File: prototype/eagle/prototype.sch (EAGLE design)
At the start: 45 parts, among them J4 USBSMD, T1 3904, U1 ATMEGA328, U2 ATA6631, U3 ATA6631, U5 FT232RL, X1 16MHz

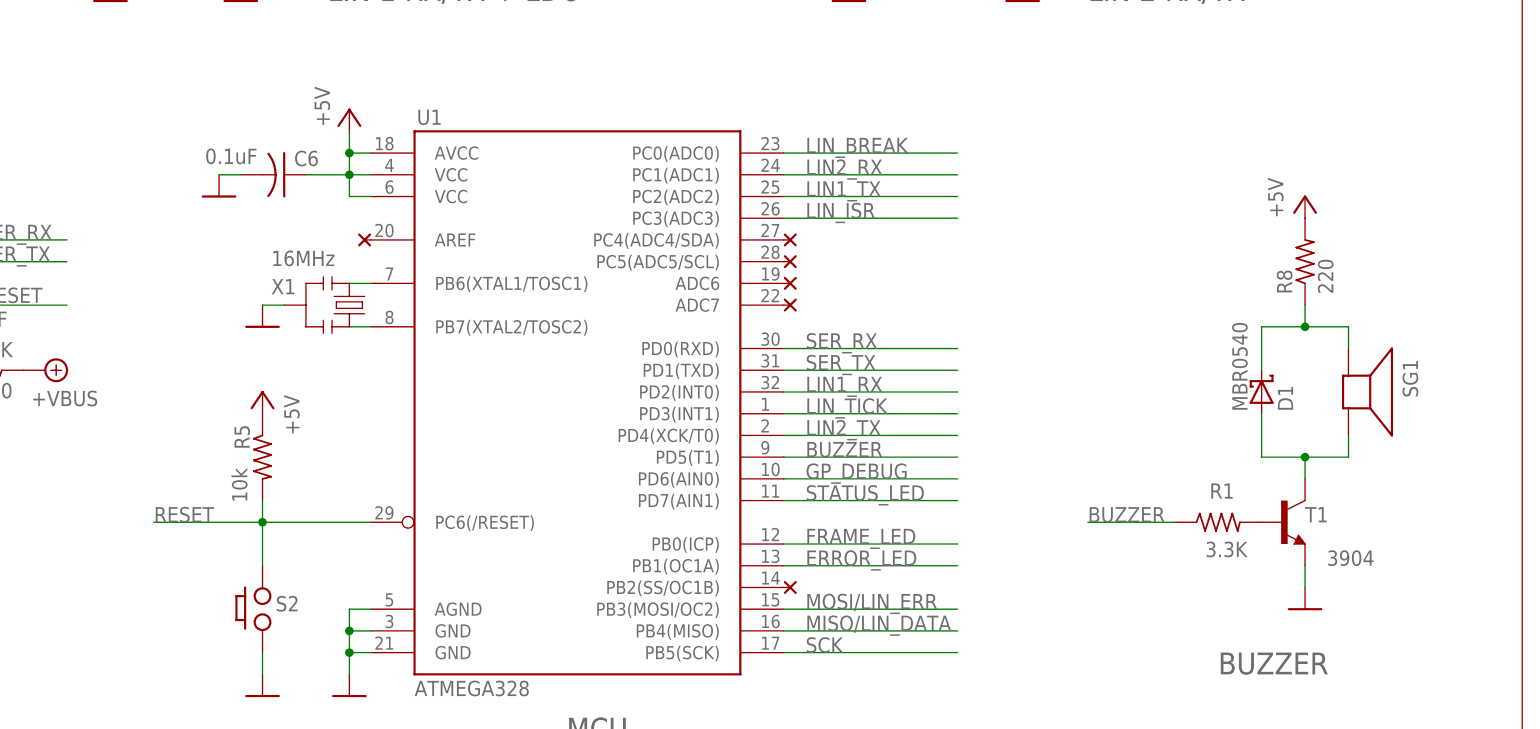
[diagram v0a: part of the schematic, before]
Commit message: Updated prototype schema. Buzzer is now fed from 12V (was 5V).
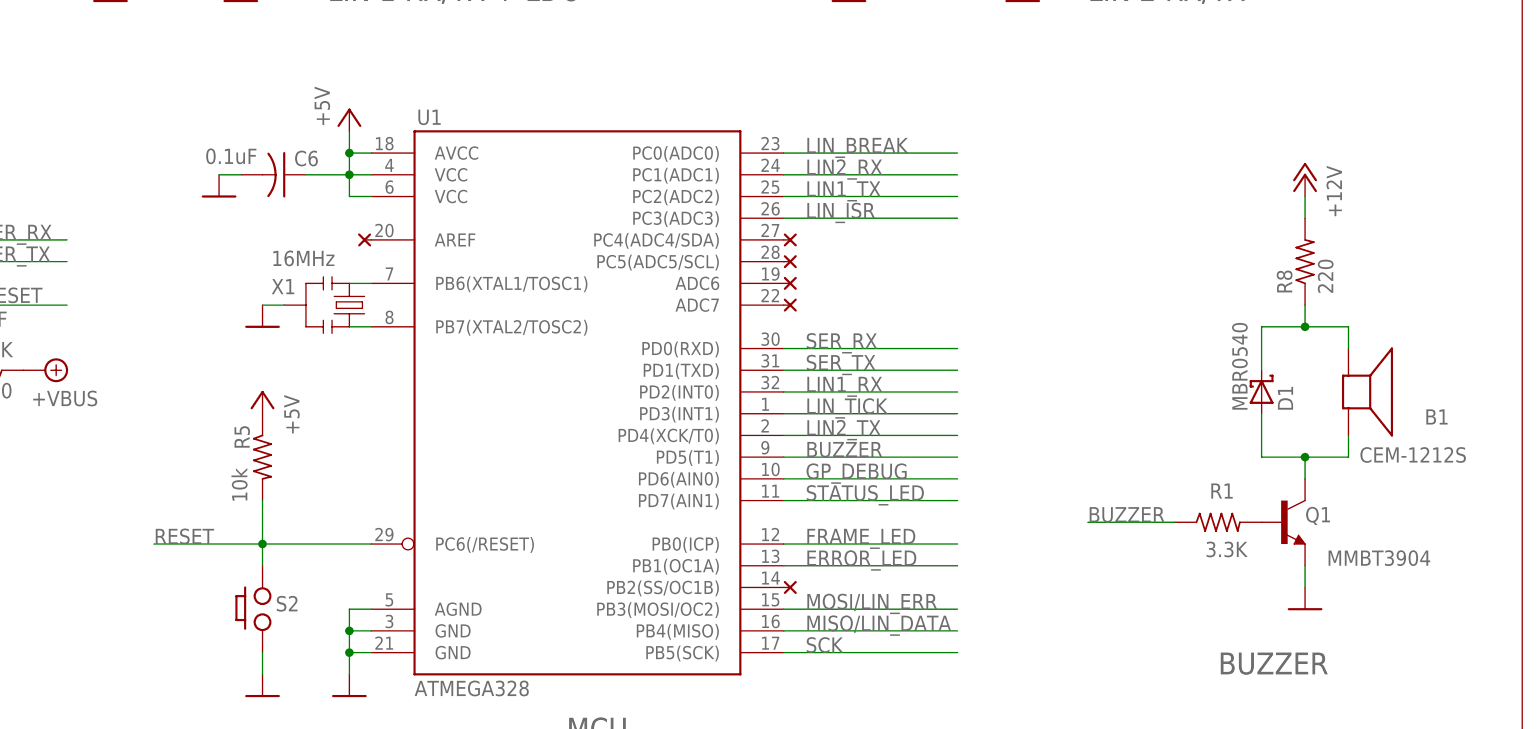
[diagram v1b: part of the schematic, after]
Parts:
- B1: value AL60P -> CEM-1212S
- Q1: value 3904 -> MMBT3904
- renumbered SG1 to B1, T1 to Q1
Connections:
- net +12V: now also R8.2
- net +5V: no longer R8.2
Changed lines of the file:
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@@
 <part name="GND14" library="prototype" deviceset="GND" device=""/>
 <part name="P+5" library="prototype" deviceset="+5V" device=""/>
-<part name="SG1" library="prototype" deviceset="AL60P" device="" value=""/>
+<part name="B1" library="prototype" deviceset="AL60P" device="" value="CEM-1212S"/>
 <part name="R1" library="prototype" deviceset="R-US_" device="R0805" value="3.3K"/>
-<part name="T1" library="prototype" deviceset="*-NPN-" device="SOT23-BEC" technology="MMBT3904LT1" value="3904"/>
+<part name="Q1" library="prototype" deviceset="*-NPN-" device="SOT23-BEC" technology="MMBT3904LT1" value="MMBT3904"/>
 <part name="GND18" library="prototype" deviceset="GND" device=""/>
 <part name="D1" library="prototype" deviceset="SMF5.0AT1" device="" value="MBR0540"/>
-<part name="P+3" library="prototype" deviceset="+5V" device=""/>
 <part name="R8" library="prototype" deviceset="R-US_" device="R0805" value="220"/>
 <part name="GND10" library="prototype" deviceset="GND" device=""/>
@@
 <part name="C6" library="prototype" deviceset="C-US" device="C0805" value="0.1uF"/>
 <part name="GND30" library="prototype" deviceset="GND" device=""/>
+<part name="P+3" library="prototype" deviceset="+12V" device=""/>
 </parts>
 <sheets>
@@
 <attribute name="VALUE" x="190.5" y="60.198" size="1.778" layer="96" rot="MR90"/>
 </instance>
-<instance part="SG1" gate="G$1" x="289.56" y="114.3" rot="R270"/>
+<instance part="B1" gate="G$1" x="289.56" y="114.3" smashed="yes" rot="R270">
+<attribute name="NAME" x="298.45" y="110.49" size="1.778" layer="95"/>
+<attribute name="VALUE" x="290.83" y="106.045" size="1.778" layer="96"/>
+</instance>
 <instance part="R1" gate="G$1" x="274.32" y="99.06" smashed="yes">
 <attribute name="NAME" x="273.304" y="101.8286" size="1.778" layer="95"/>
 <attribute name="VALUE" x="272.796" y="94.996" size="1.778" layer="96"/>
 </instance>
-<instance part="T1" gate="G$1" x="281.94" y="99.06" smashed="yes">
+<instance part="Q1" gate="G$1" x="281.94" y="99.06" smashed="yes">
 <attribute name="NAME" x="284.48" y="99.06" size="1.778" layer="95"/>
 <attribute name="VALUE" x="287.02" y="93.98" size="1.778" layer="96"/>
@@
 <instance part="GND18" gate="1" x="284.48" y="88.9"/>
 <instance part="D1" gate="G$1" x="279.4" y="114.3" rot="MR90"/>
-<instance part="P+3" gate="1" x="284.48" y="137.16" smashed="yes">
-<attribute name="VALUE" x="281.94" y="134.62" size="1.778" layer="96" rot="R90"/>
-</instance>
 <instance part="R8" gate="G$1" x="284.48" y="129.54" rot="R90"/>
 <instance part="GND10" gate="1" x="160.02" y="160.02"/>
@@
 </instance>
 <instance part="GND30" gate="1" x="157.48" y="137.16"/>
+<instance part="P+3" gate="1" x="284.48" y="139.7" rot="MR0"/>
 </instances>
 <busses>
@@
 </segment>
 <segment>
-<pinref part="T1" gate="G$1" pin="E"/>
+<pinref part="Q1" gate="G$1" pin="E"/>
 <pinref part="GND18" gate="1" pin="GND"/>
 <wire x1="284.48" y1="93.98" x2="284.48" y2="91.44" width="0.1524" layer="91"/>
@@
 <wire x1="111.76" y1="152.4" x2="119.38" y2="152.4" width="0.1524" layer="91"/>
 </segment>
+<segment>
+<pinref part="P+3" gate="1" pin="+12V"/>
+<pinref part="R8" gate="G$1" pin="2"/>
+<wire x1="284.48" y1="137.16" x2="284.48" y2="134.62" width="0.1524" layer="91"/>
+</segment>
 </net>
 <net name="+5V" class="0">
@@
 <wire x1="177.8" y1="58.42" x2="187.96" y2="58.42" width="0.1524" layer="91"/>
 <wire x1="187.96" y1="58.42" x2="187.96" y2="60.96" width="0.1524" layer="91"/>
-</segment>
-<segment>
-<pinref part="P+3" gate="1" pin="+5V"/>
-<pinref part="R8" gate="G$1" pin="2"/>
 </segment>
 <segment>
@@
 <pinref part="D1" gate="G$1" pin="A"/>
 <wire x1="279.4" y1="111.76" x2="279.4" y2="106.68" width="0.1524" layer="91"/>
-<pinref part="T1" gate="G$1" pin="C"/>
+<pinref part="Q1" gate="G$1" pin="C"/>
 <wire x1="279.4" y1="106.68" x2="284.48" y2="106.68" width="0.1524" layer="91"/>
 <wire x1="284.48" y1="106.68" x2="284.48" y2="104.14" width="0.1524" layer="91"/>
-<pinref part="SG1" gate="G$1" pin="2"/>
+<pinref part="B1" gate="G$1" pin="2"/>
 <wire x1="284.48" y1="106.68" x2="289.56" y2="106.68" width="0.1524" layer="91"/>
 <wire x1="289.56" y1="106.68" x2="289.56" y2="109.22" width="0.1524" layer="91"/>
@@
 <net name="N$19" class="0">
 <segment>
-<pinref part="T1" gate="G$1" pin="B"/>
+<pinref part="Q1" gate="G$1" pin="B"/>
 <pinref part="R1" gate="G$1" pin="2"/>
 </segment>
@@
 <pinref part="D1" gate="G$1" pin="C"/>
 <wire x1="279.4" y1="116.84" x2="279.4" y2="121.92" width="0.1524" layer="91"/>
-<pinref part="SG1" gate="G$1" pin="1"/>
+<pinref part="B1" gate="G$1" pin="1"/>
 <wire x1="279.4" y1="121.92" x2="284.48" y2="121.92" width="0.1524" layer="91"/>
 <wire x1="284.48" y1="121.92" x2="289.56" y2="121.92" width="0.1524" layer="91"/>
@@
 <segment>
 <pinref part="U1" gate="G$1" pin="PC6(/RESET)"/>
-<wire x1="175.26" y1="99.06" x2="162.56" y2="99.06" width="0.1524" layer="91"/>
+<wire x1="175.26" y1="96.52" x2="162.56" y2="96.52" width="0.1524" layer="91"/>
 <pinref part="R5" gate="G$1" pin="2"/>
 <pinref part="S2" gate="G$1" pin="P$3"/>
-<wire x1="162.56" y1="99.06" x2="149.86" y2="99.06" width="0.1524" layer="91"/>
-<wire x1="162.56" y1="101.6" x2="162.56" y2="99.06" width="0.1524" layer="91"/>
-<junction x="162.56" y="99.06"/>
-<wire x1="162.56" y1="99.06" x2="162.56" y2="93.98" width="0.1524" layer="91"/>
-<label x="149.86" y="99.06" size="1.778" layer="95"/>
-</segment>
-</net>
+<wire x1="162.56" y1="96.52" x2="149.86" y2="96.52" width="0.1524" layer="91"/>
+<wire x1="162.56" y1="101.6" x2="162.56" y2="96.52" width="0.1524" layer="91"/>
+<junction x="162.56" y="96.52"/>
+<wire x1="162.56" y1="96.52" x2="162.56" y2="93.98" width="0.1524" layer="91"/>
+<label x="149.86" y="96.52" size="1.778" layer="95"/>
+</segment>
+</net>

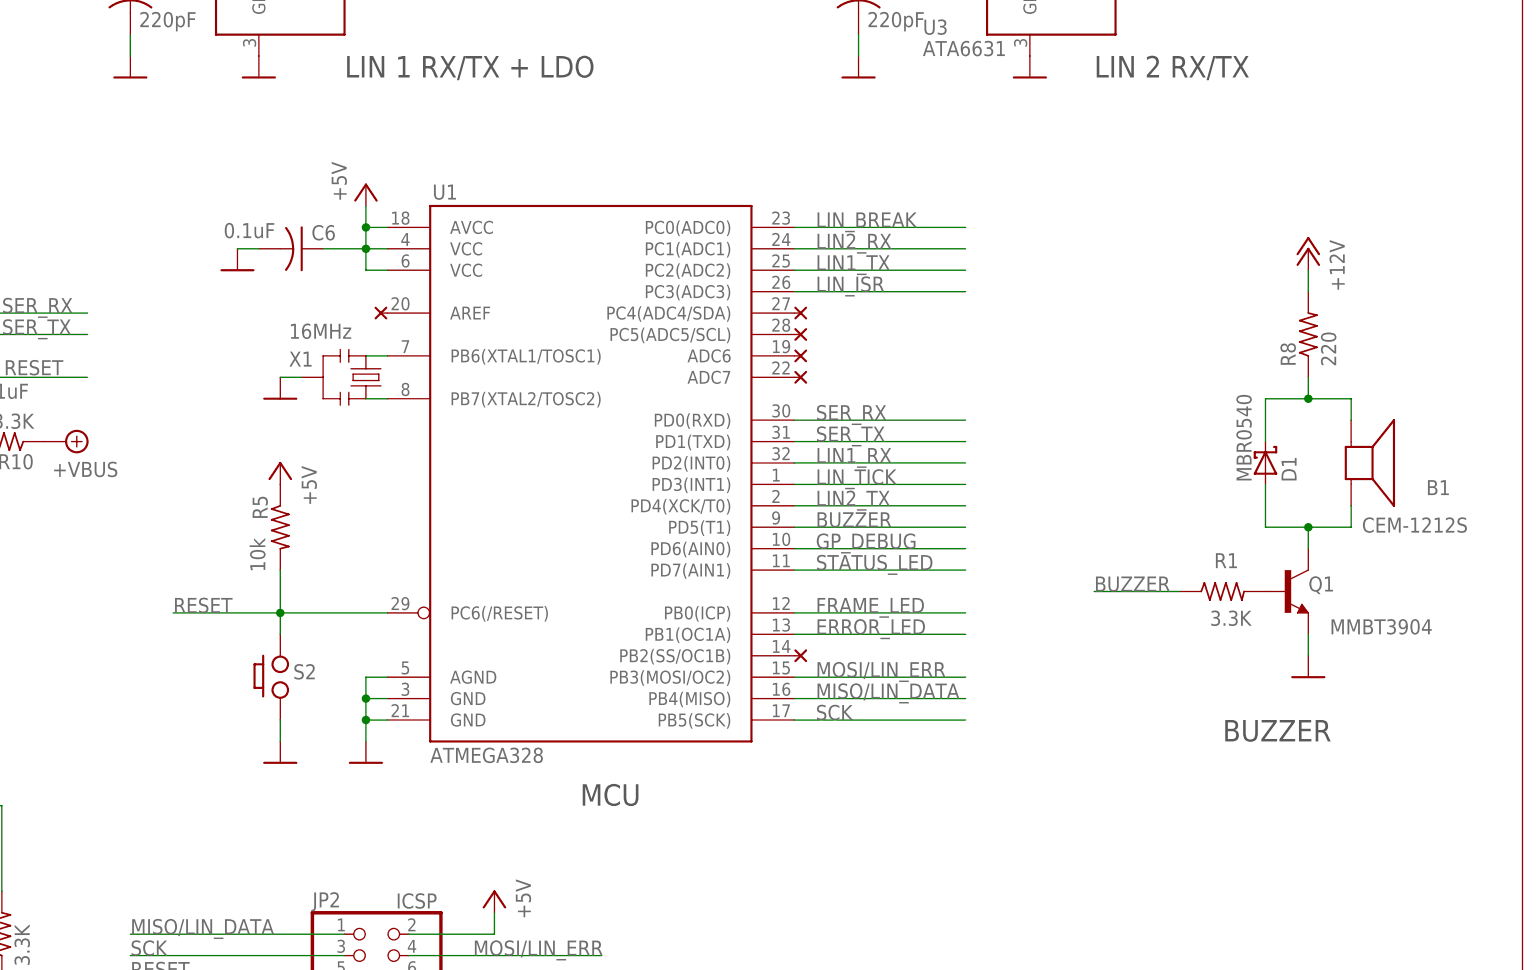
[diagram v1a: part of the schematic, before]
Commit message: Added a working injector logic. Tweaked the schematic.
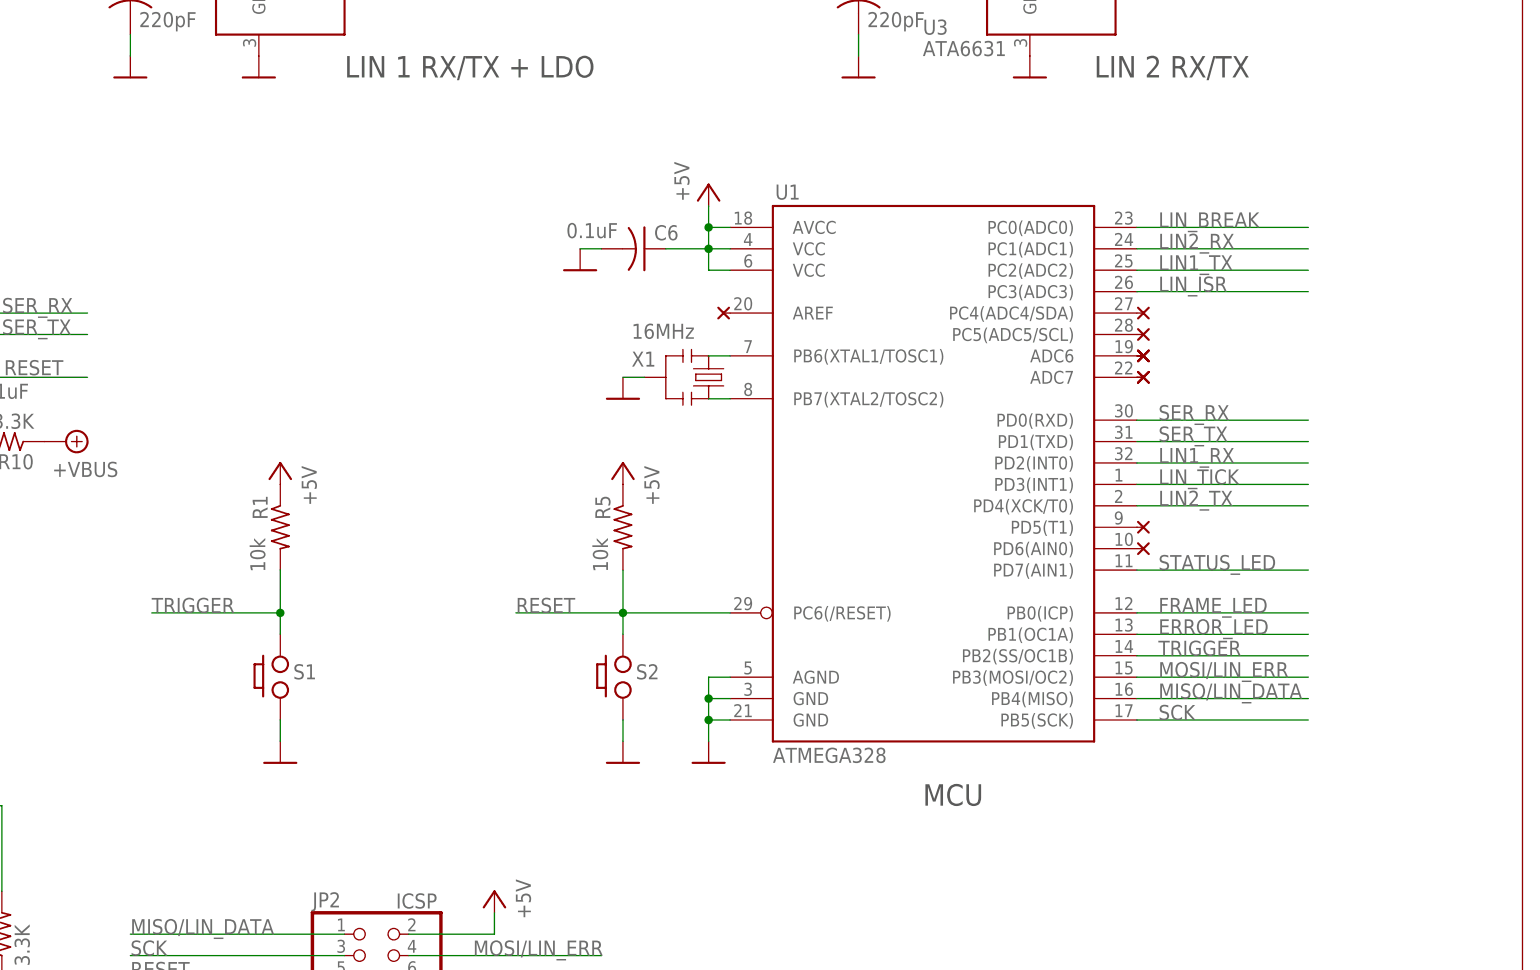
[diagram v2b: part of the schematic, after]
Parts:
- removed B1: CEM-1212S, prototype:AL60P
- removed D1: MBR0540, prototype:SMF5.0AT1
- removed Q1: MMBT3904, prototype:MMBT3904LT1-NPN-SOT23-BEC
- removed R8: 220, prototype:R-US_R0805
- added S1: PUSH_BUTTON, prototype:PUSH_BUTTON
- R1: value 3.3K -> 10k
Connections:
- removed net BUZZER: R1.1, U1.PD5(T1)
- removed net N$19: Q1.B, R1.2
- removed net N$30: B1.1, D1.C, R8.1
- removed net N$31: B1.2, D1.A, Q1.C
- new net TRIGGER: R1.2, S1.P$3, U1.PB2(SS/OC1B)
- net +12V: no longer R8.2
- net +5V: now also R1.1
- net GND: now also S1.P$4; no longer Q1.E
- net GP_DEBUG: no longer U1.PD6(AIN0)
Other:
- note removed: "BUZZER"
- moved on the sheet: C6, R1, R5, S2, U1, X1
